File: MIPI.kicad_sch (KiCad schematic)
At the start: 10 parts, among them IC1 ECP5-BGA256, J2 Conn_01x15, J3 USB_B_Micro

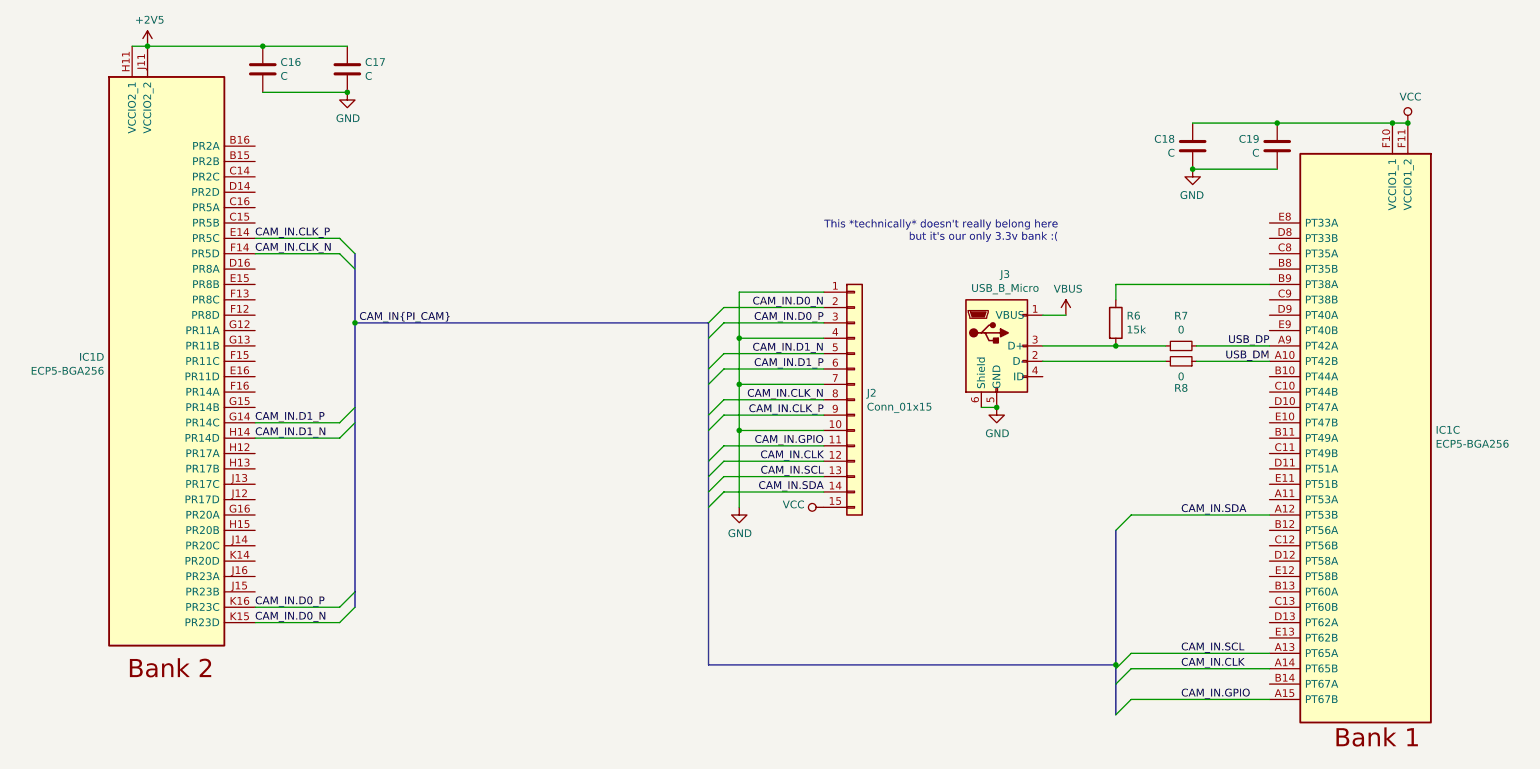
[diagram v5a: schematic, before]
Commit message: Remove SD card, relocate regulators
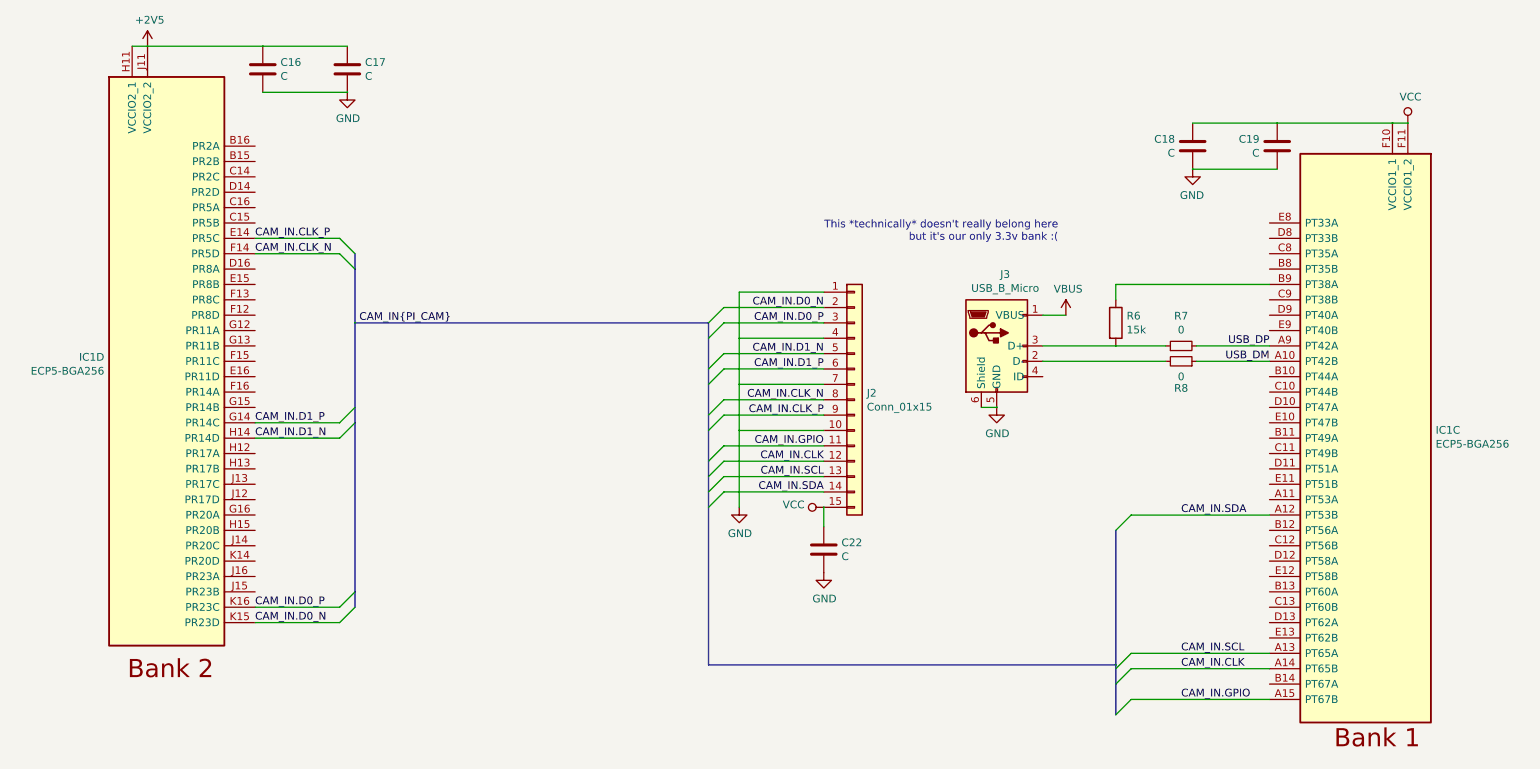
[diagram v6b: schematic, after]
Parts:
- added C22: C, Capacitor_SMD:C_0805_2012Metric, symbol Device:C
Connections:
- net GND: now also C22.2
- net VCC: now also C22.1
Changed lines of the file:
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@@
-(kicad_sch (version 20200714) (host eeschema "5.99.0-unknown-8324cb3~102~ubuntu20.04.1")
-  (page 1 6)
+(kicad_sch (version 20200714) (host eeschema "5.99.0-unknown-027b6c8cf~102~ubuntu20.04.1")
+  (page 2 6)
   (paper "A4")
   (bus_alias "PI_CAM" (members "D0_P" "D0_N" "D1_P" "D1_N" "CLK_P" "CLK_N" "GPIO" "CLK" "SCL" "SDA"))
-  (junction (at 43.18 29.21) (diameter 0) (color 0 0 0 0))
-  (junction (at 62.23 29.21) (diameter 0) (color 0 0 0 0))
-  (junction (at 76.2 36.83) (diameter 0) (color 0 0 0 0))
-  (junction (at 140.97 77.47) (diameter 0) (color 0 0 0 0))
-  (junction (at 140.97 85.09) (diameter 0) (color 0 0 0 0))
-  (junction (at 140.97 92.71) (diameter 0) (color 0 0 0 0))
-  (junction (at 183.515 88.9) (diameter 0) (color 0 0 0 0))
-  (junction (at 203.2 78.74) (diameter 0) (color 0 0 0 0))
-  (junction (at 215.9 49.53) (diameter 0) (color 0 0 0 0))
-  (junction (at 229.87 41.91) (diameter 0) (color 0 0 0 0))
-  (junction (at 248.92 41.91) (diameter 0) (color 0 0 0 0))
-  (junction (at 251.46 41.91) (diameter 0) (color 0 0 0 0))
-  (junction (at 77.47 74.93) (diameter 0) (color 0 0 0 0))
-  (junction (at 203.2 131.445) (diameter 0) (color 0 0 0 0))
+  (junction (at 43.18 29.21) (diameter 0.3048) (color 0 0 0 0))
+  (junction (at 62.23 29.21) (diameter 0.3048) (color 0 0 0 0))
+  (junction (at 76.2 36.83) (diameter 0.3048) (color 0 0 0 0))
+  (junction (at 140.97 77.47) (diameter 0.3048) (color 0 0 0 0))
+  (junction (at 140.97 85.09) (diameter 0.3048) (color 0 0 0 0))
+  (junction (at 140.97 92.71) (diameter 0.3048) (color 0 0 0 0))
+  (junction (at 154.94 105.41) (diameter 0.3048) (color 0 0 0 0))
+  (junction (at 183.515 88.9) (diameter 0.3048) (color 0 0 0 0))
+  (junction (at 203.2 78.74) (diameter 0.3048) (color 0 0 0 0))
+  (junction (at 215.9 49.53) (diameter 0.3048) (color 0 0 0 0))
+  (junction (at 229.87 41.91) (diameter 0.3048) (color 0 0 0 0))
+  (junction (at 248.92 41.91) (diameter 0.3048) (color 0 0 0 0))
+  (junction (at 251.46 41.91) (diameter 0.3048) (color 0 0 0 0))
+  (junction (at 77.47 74.93) (diameter 0.3048) (color 0 0 0 0))
+  (junction (at 203.2 131.445) (diameter 0.3048) (color 0 0 0 0))
   (bus_entry (at 74.93 60.96) (size 2.54 2.54)
     (stroke (width 0.1524) (type solid) (color 0 0 0 0))
@@
     (stroke (width 0) (type solid) (color 0 0 0 0))
   )
+  (wire (pts (xy 154.94 105.41) (xy 154.94 108.585))
+    (stroke (width 0) (type solid) (color 0 0 0 0))
+  )
   (wire (pts (xy 180.975 88.9) (xy 183.515 88.9))
     (stroke (width 0) (type solid) (color 0 0 0 0))
@@
     (stroke (width 0) (type solid) (color 0 0 0 0))
   )
-  (bus (pts (xy 77.47 63.5) (xy 77.47 74.93))
+  (bus (pts (xy 77.47 63.5) (xy 77.47 66.04))
+    (stroke (width 0) (type solid) (color 0 0 0 0))
+  )
+  (bus (pts (xy 77.47 66.04) (xy 77.47 74.93))
     (stroke (width 0) (type solid) (color 0 0 0 0))
   )
@@
     (stroke (width 0) (type solid) (color 0 0 0 0))
   )
-  (bus (pts (xy 77.47 88.9) (xy 77.47 119.38))
+  (bus (pts (xy 77.47 88.9) (xy 77.47 91.44))
+    (stroke (width 0) (type solid) (color 0 0 0 0))
+  )
+  (bus (pts (xy 77.47 91.44) (xy 77.47 119.38))
     (stroke (width 0) (type solid) (color 0 0 0 0))
   )
@@
     (stroke (width 0) (type solid) (color 0 0 0 0))
   )
-  (bus (pts (xy 135.89 74.93) (xy 135.89 82.55))
-    (stroke (width 0) (type solid) (color 0 0 0 0))
-  )
-  (bus (pts (xy 135.89 82.55) (xy 135.89 90.17))
-    (stroke (width 0) (type solid) (color 0 0 0 0))
-  )
-  (bus (pts (xy 135.89 90.17) (xy 135.89 97.79))
-    (stroke (width 0) (type solid) (color 0 0 0 0))
-  )
-  (bus (pts (xy 135.89 97.79) (xy 135.89 102.87))
-    (stroke (width 0) (type solid) (color 0 0 0 0))
-  )
-  (bus (pts (xy 135.89 102.87) (xy 135.89 131.445))
+  (bus (pts (xy 135.89 74.93) (xy 135.89 77.47))
+    (stroke (width 0) (type solid) (color 0 0 0 0))
+  )
+  (bus (pts (xy 135.89 77.47) (xy 135.89 82.55))
+    (stroke (width 0) (type solid) (color 0 0 0 0))
+  )
+  (bus (pts (xy 135.89 82.55) (xy 135.89 85.09))
+    (stroke (width 0) (type solid) (color 0 0 0 0))
+  )
+  (bus (pts (xy 135.89 85.09) (xy 135.89 90.17))
+    (stroke (width 0) (type solid) (color 0 0 0 0))
+  )
+  (bus (pts (xy 135.89 90.17) (xy 135.89 92.71))
+    (stroke (width 0) (type solid) (color 0 0 0 0))
+  )
+  (bus (pts (xy 135.89 92.71) (xy 135.89 97.79))
+    (stroke (width 0) (type solid) (color 0 0 0 0))
+  )
+  (bus (pts (xy 135.89 97.79) (xy 135.89 100.33))
+    (stroke (width 0) (type solid) (color 0 0 0 0))
+  )
+  (bus (pts (xy 135.89 100.33) (xy 135.89 102.87))
+    (stroke (width 0) (type solid) (color 0 0 0 0))
+  )
+  (bus (pts (xy 135.89 102.87) (xy 135.89 105.41))
+    (stroke (width 0) (type solid) (color 0 0 0 0))
+  )
+  (bus (pts (xy 135.89 105.41) (xy 135.89 131.445))
     (stroke (width 0) (type solid) (color 0 0 0 0))
   )
@@
     (stroke (width 0) (type solid) (color 0 0 0 0))
   )
-  (bus (pts (xy 203.2 131.445) (xy 203.2 134.62))
+  (bus (pts (xy 203.2 131.445) (xy 203.2 132.08))
+    (stroke (width 0) (type solid) (color 0 0 0 0))
+  )
+  (bus (pts (xy 203.2 132.08) (xy 203.2 134.62))
     (stroke (width 0) (type solid) (color 0 0 0 0))
   )
@@
     )
     (property "Datasheet" "" (id 3) (at 140.97 105.41 0)
+      (effects (font (size 1.27 1.27)) hide)
+    )
+  )
+  (symbol (lib_id "power:GND") (at 154.94 116.205 0) (unit 1)
+    (in_bom yes) (on_board yes)
+    (property "Reference" "#PWR0151" (id 0) (at 154.94 122.555 0)
+      (effects (font (size 1.27 1.27)) hide)
+    )
+    (property "Value" "GND" (id 1) (at 155.0543 120.5294 0))
+    (property "Footprint" "" (id 2) (at 154.94 116.205 0)
+      (effects (font (size 1.27 1.27)) hide)
+    )
+    (property "Datasheet" "" (id 3) (at 154.94 116.205 0)
       (effects (font (size 1.27 1.27)) hide)
     )
@@
       (effects (font (size 1.27 1.27)) hide)
     )
+  )
+  (symbol (lib_id "Device:C") (at 154.94 112.395 0) (unit 1)
+    (in_bom yes) (on_board yes)
+    (property "Reference" "C22" (id 0) (at 157.8611 111.2456 0)
+      (effects (font (size 1.27 1.27)) (justify left))
+    )
+    (property "Value" "C" (id 1) (at 157.8611 113.5443 0)
+      (effects (font (size 1.27 1.27)) (justify left))
+    )
+    (property "Footprint" "Capacitor_SMD:C_0805_2012Metric" (id 2) (at 155.9052 116.205 0)
+      (effects (font (size 1.27 1.27)) hide)
+    )
+    (property "Datasheet" "~" (id 3) (at 154.94 112.395 0)
+      (effects (font (size 1.27 1.27)) hide)
+    )
